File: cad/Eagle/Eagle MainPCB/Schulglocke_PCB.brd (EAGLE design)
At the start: 100 x 100 mm, 33 parts, among them K1 JS-M1-9V-5, M1 DS3231SHIELD, M2 EMC28J60SHIELD, M3 WAVESHAREDISPLAY, Q1 BSS123, Q2 BSS123

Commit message: leiterplatte plaziert
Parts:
- removed B1: ARDUINO_MEGA_R3FULL, sparkfun eagle:ARDUINO_MEGA_NO_SILK
- removed K1: JS-M1-9V-5, relay:JS-M
- removed S1: (no value), switch:255SB
- added B2: ARDUINO_MEGA_R3_CUSTOM_SHIELDFULL, customlib:ARDUINO_MEGA_NO_SILK
- added C5: (no value), rcl:C1206K
- added REL1: (no value), special:REL-5PIN
- F1, F2: value FUSEBLANK_5X20MM -> (none); device fuse:FUSE_HOLDER_5X20MM -> special:FUSE1
- moved D3 297.1 mm to (131.9, 33.1)
- moved Q2 275.1 mm to (133.9, 23.8), turned to 270 degrees
- moved R8 253.7 mm to (127.4, 24.0), turned to 180 degrees
- moved LED2 247.7 mm to (125.4, 61.6), turned to 180 degrees
- moved F2 237.2 mm to (67.2, 19.0), flipped to the bottom, turned to 90 degrees
- moved LED1 235.8 mm to (125.4, 67.7), turned to 180 degrees
- moved C3 233.9 mm to (89.8, 9.24), turned to 90 degrees
- moved D1 233.9 mm to (79.2, 29.6), turned to 180 degrees
- moved C2 233.5 mm to (105.1, 11.0), flipped to the bottom, turned to 90 degrees
- moved R7 220.8 mm to (119.7, 61.6)
- moved R6 219.9 mm to (119.8, 56.0), turned to 180 degrees
- moved R10 211.6 mm to (96.9, 6.01), flipped to the bottom, turned to 180 degrees
- moved R9 211.6 mm to (113.2, 11.6), flipped to the bottom, turned to 180 degrees
- moved C1 210.0 mm to (114.3, 28.2), turned to 90 degrees
- moved D2 206.7 mm to (21.4, 21.8), turned to 270 degrees
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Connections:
- removed net N$11: JP1.2, S1.2
- new net N$18: B2.30
- net +3V3: now also B2.3.3V; no longer B1.3.3V
- net +5V: now also B2.5V, B2.5V@1, B2.5V@2; no longer B1.5V, B1.5V@1, B1.5V@2
- net ARD_MISO: now also B2.50; no longer B1.50
- net ARD_MOSI: now also B2.51; no longer B1.51
- net ARD_SCK: now also B2.52; no longer B1.52
- net ARD_SCL: now also B2.SCL; no longer B1.SCL
- net ARD_SDA: now also B2.SDA; no longer B1.SDA
- net ETH_CS: now also B2.28; no longer B1.28
- net GND: now also B2.GND, B2.GND@1, B2.GND@2, B2.GND@3, B2.GND@4, C5.2; no longer B1.GND, B1.GND@1, B1.GND@2, B1.GND@3, B1.GND@4
- net LCD_BL: now also B2.9; no longer B1.9
- net LCD_CS: now also B2.10; no longer B1.10
- net LCD_DC: now also B2.7; no longer B1.7
- net LCD_RST: now also B2.8; no longer B1.8
- net N$1: now also REL1.C; no longer K1.C
- net N$10: now also REL1.S1; no longer K1.2
- net N$12: now also B2.24; no longer B1.24
- net N$16: now also B2.22, R3.1; no longer B1.22
- net N$17: no longer R3.1
- net N$2: now also REL1.O; no longer K1.NC
- net N$3: now also REL1.S; no longer K1.NO
- net N$4: now also F1.2A; no longer F2.2
- net N$8: now also F1.1A, F2.1A, JP1.2; no longer F1.1, F2.1, S1.3
- net N$9: now also F2.2A; no longer F1.2
- net OPT_ISOL: now also B2.26; no longer B1.26
- net SD_CS: now also B2.5; no longer B1.5
- net TP_BUSY: now also B2.6; no longer B1.6
- net TP_CS: now also B2.4; no longer B1.4
- net TP_IRQ: now also B2.3; no longer B1.3
- net VCC: now also B2.VIN, C5.1, REL1.S2; no longer B1.VIN, K1.1
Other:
- board size 100 x 100 mm -> 140 x 90 mm
- board text added: "Grid Sizes 1mm 0.2mm 100mil 10mil"

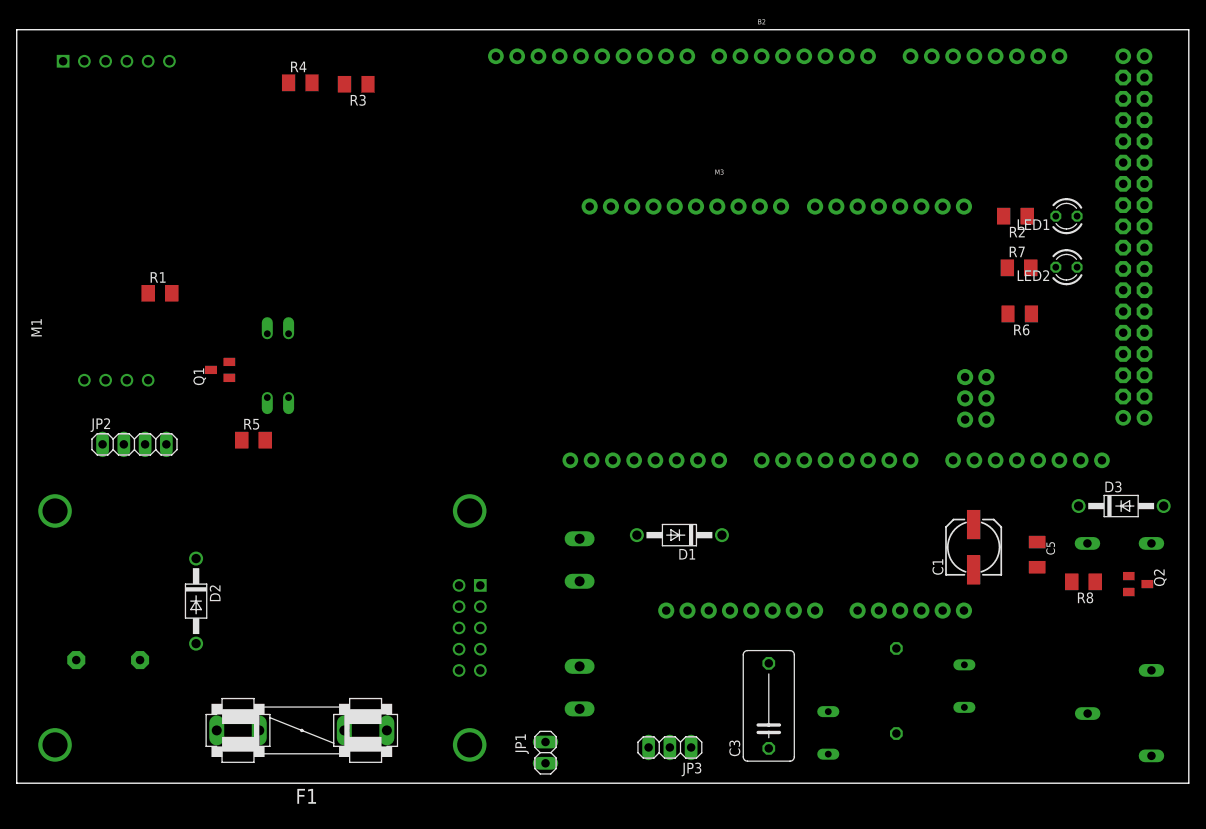
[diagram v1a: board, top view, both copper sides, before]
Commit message: mit traces noch ohne montagelöcher und ohne anpassung footprints
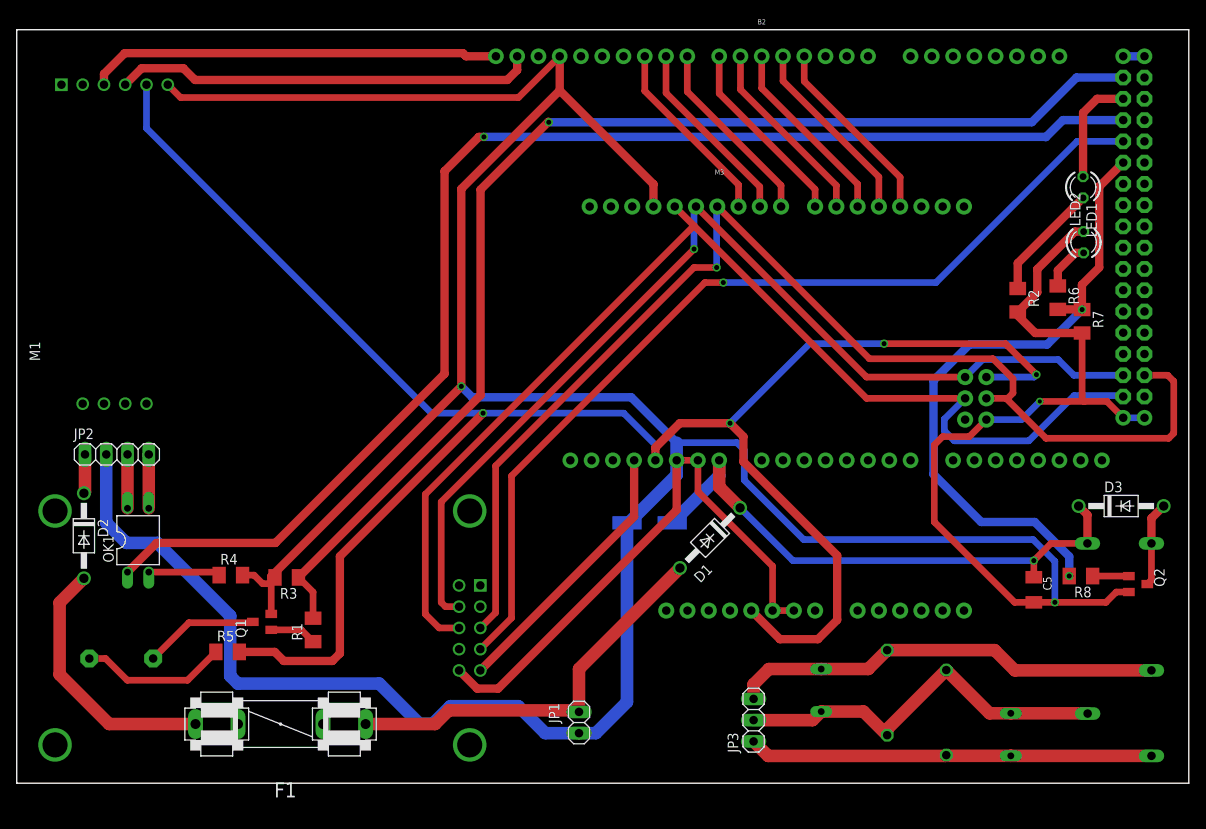
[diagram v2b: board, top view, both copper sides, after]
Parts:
- removed F2: (no value), special:FUSE1
- moved R3 59.5 mm to (32.2, 24.6)
- moved R4 59.4 mm to (25.6, 24.9)
- moved R1 44.2 mm to (35.4, 18.3), turned to 90 degrees
- moved C1 38.8 mm to (75.6, 31.1), flipped to the bottom, turned to 180 degrees
- moved Q1 30.5 mm to (29.3, 19.3)
- moved OK1 26.7 mm to (14.5, 29.0), flipped to the top, turned to 0 degrees
- moved R5 25.5 mm to (25.2, 15.7)
- moved R10 21.8 mm to (118.7, 5.81)
- moved C3 21.2 mm to (111.0, 8.44), flipped to the bottom
- moved R9 17.1 mm to (96.1, 11.1)
- moved D2 15.5 mm to (8.02, 29.6)
- moved JP3 10.5 mm to (88.0, 7.53), turned to 90 degrees
- moved R2 10.0 mm to (119.6, 57.7), turned to 270 degrees
- moved R7 9.87 mm to (127.3, 55.2), turned to 270 degrees
- moved JP1 5.38 mm to (67.2, 7.25)
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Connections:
- removed net N$18: B2.30
- removed net N$8: F1.1A, F2.1A, JP1.2
- net N$9: now also F1.1A, JP1.2; no longer F2.2A
- net RELAY_EN: now also B2.30
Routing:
- net GND: track 0.00 -> 526.0 mm, vias 0 -> 3
- net +5V: track 0.00 -> 235.9 mm, vias 0 -> 4
- net OPT_ISOL: track 0.00 -> 155.5 mm, vias 0 -> 1
- net ARD_MOSI: track 0.00 -> 144.9 mm, vias 0 -> 1
- net N$16: track 0.00 -> 143.3 mm, vias 0 -> 1
- net ARD_SCK: track 0.00 -> 137.6 mm
- net ARD_MISO: track 0.00 -> 123.3 mm, vias 0 -> 1
- net ETH_CS: track 0.00 -> 111.9 mm, vias 0 -> 1
- net RELAY_EN: track 0.00 -> 77.6 mm, vias 0 -> 2
- net VCC: track 0.00 -> 68.3 mm, vias 0 -> 1
- net N$3: track 0.00 -> 52.0 mm
- net ARD_SDA: track 0.00 -> 50.4 mm
- net ARD_SCL: track 0.00 -> 49.3 mm
- net N$9: track 0.00 -> 48.4 mm
- net N$2: track 0.00 -> 48.3 mm
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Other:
- board text added: "PCB DIMENTIONS min trace with and spacing 5mil (0.127mm) Trace to Outline 0.2mm Pth min 0.2 Min. Via hole size 0.3mm Min. Via diameter 0.4mm"
- board text added: "trcace sizes 0.2mm 0.4mm 0.8mm 1mm 1.5mm"

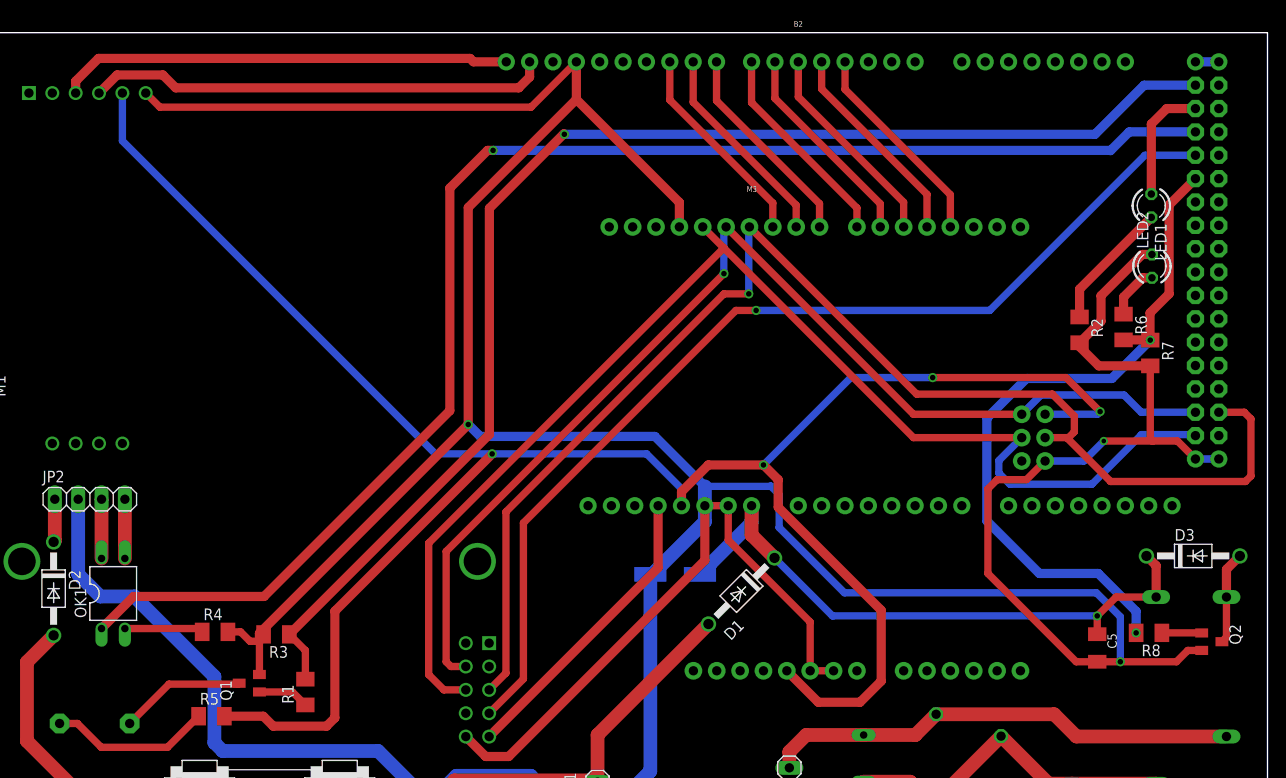
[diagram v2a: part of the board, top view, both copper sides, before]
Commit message: added drill holes
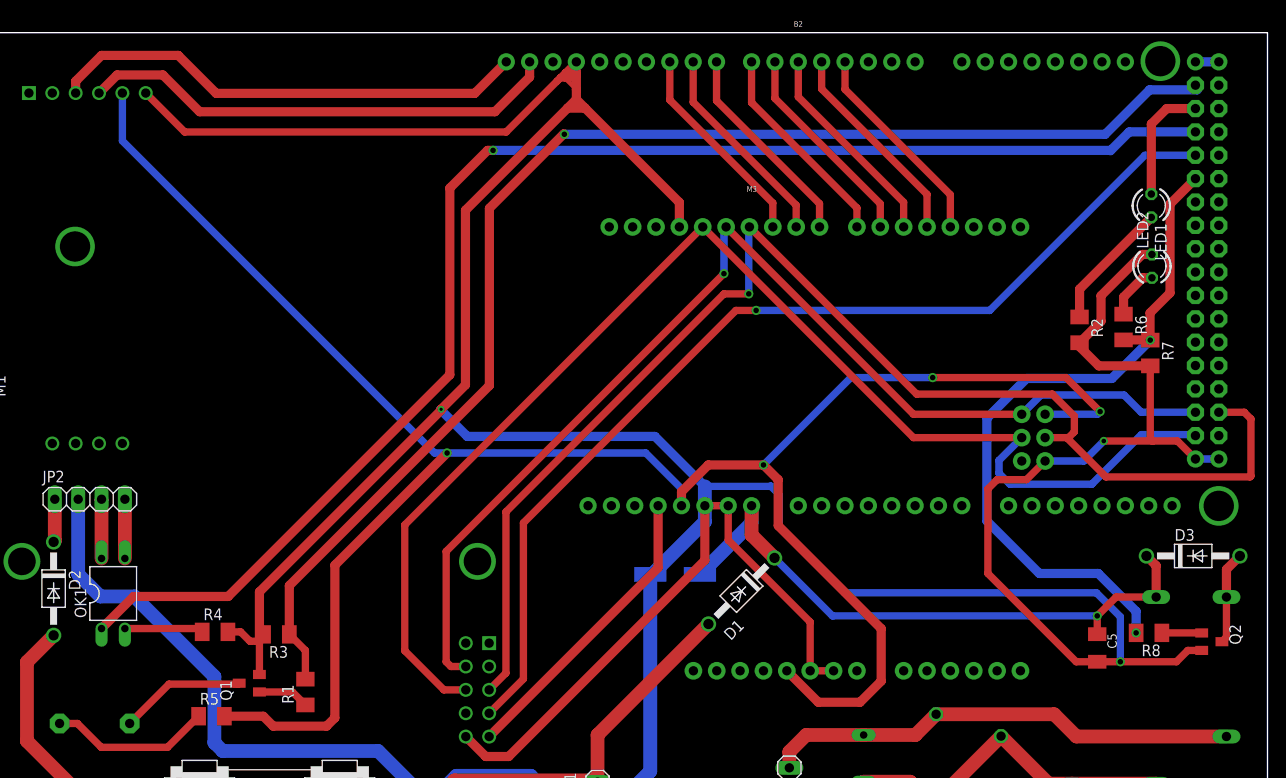
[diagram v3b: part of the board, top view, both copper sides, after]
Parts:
- added U$1, U$2, U$3: MOUNTPOINT3.3MM, customlib:MOUNT_POINT_3.3MM
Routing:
- net GND: track 526.0 -> 538.8 mm
- net ARD_SCK: track 137.6 -> 141.1 mm
- net ARD_SCL: track 49.3 -> 52.4 mm
- net OPT_ISOL: track 155.5 -> 153.2 mm
- net ARD_SDA: track 50.4 -> 52.5 mm
- net +5V: track 235.9 -> 234.0 mm
- net N$16: track 143.3 -> 143.9 mm

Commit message: changed ds clock layou
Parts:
- moved U$3 10.9 mm to (15.2, 57.0)
- moved M1 0.72 mm to (10.4, 59.9)
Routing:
- net +5V: track 234.0 -> 232.4 mm
- net ARD_SDA: track 52.5 -> 53.2 mm
- net ARD_SCL: track 52.4 -> 53.1 mm
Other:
- board text added: "1"
- board text added: "2"
- board text added: "Michael Schima Viktor Mandelbauer 2022 / 2023"
